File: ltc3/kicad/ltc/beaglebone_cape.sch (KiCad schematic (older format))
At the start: 13 parts, among them P301 BeagleBone_Black_Expansion_He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, P302 BeagleBone_Black_Expansion_He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, P303 JST PH header, P304 JST PH header, U301 CAT24C256

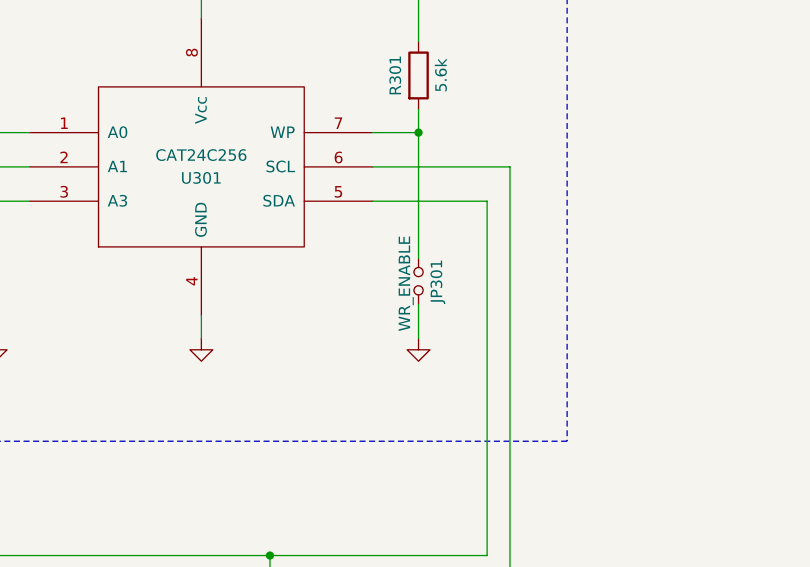
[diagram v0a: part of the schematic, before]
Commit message: LTC3: LTC schematic changes; LTC BOM work.
* Replaced LTC external power and trigger circuits' off-board manual
  override switches with board-mounted tactile momentary switches.
  Simplifies assembly, and should be more than adequate for debugging
  purposes.

* Changed cell protection diodes D1 and D6 from Rohm 1SS355 to ComChip
  CDSU4148.  CDSU4148 is already used on the LTC board, and is higher
  spec than the 1SS355.
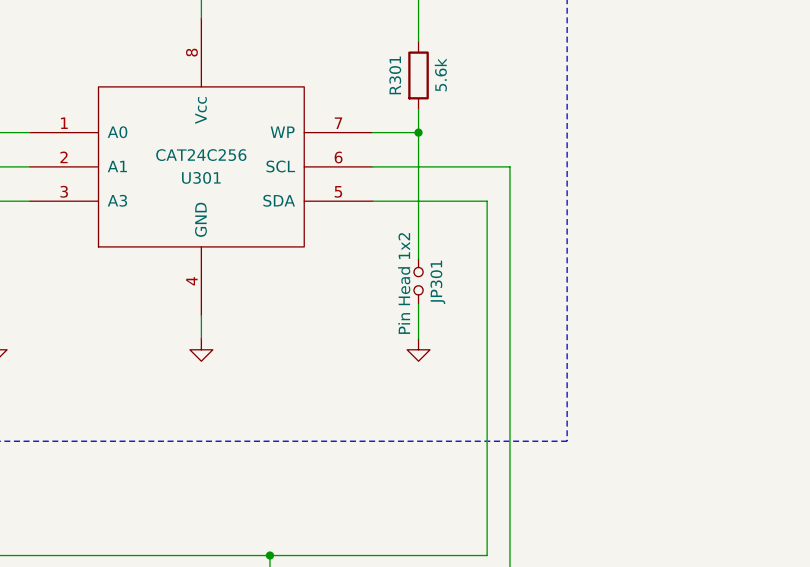
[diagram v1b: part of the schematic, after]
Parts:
- JP301: value WR_ENABLE -> Pin Head 1x2; Note Pin Header, 1x2 -> WR_ENABLE
- U301: Mfg_Name ON -> ON Semi

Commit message: LTC3: More work on LTC BOM.
Almost there!
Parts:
- P303: value JST PH header -> XH header; footprint Connectors_JST:JST_PH_B4B-PH-K_02x2.00mm_Straight -> Connectors_JST:JST_XH_B04B-XH-A_02x2.50mm_Straight; Mfg_Description - -> 4 pos vertical header; Mfg_PN B4B-PH-K-S -> B4B-XH-A(LF)(SN); Note To Charge Controller -> to charge controller
- P304: value JST PH header -> XH header; footprint Connectors_JST:JST_PH_B4B-PH-K_02x2.00mm_Straight -> Connectors_JST:JST_XH_B04B-XH-A_02x2.50mm_Straight; Mfg_Description - -> 4 pos vertical header; Mfg_PN B4B-PH-K-S -> B4B-XH-A(LF)(SN); Note To Cell Protection -> to cell protection
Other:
- note added: "TODO: add off-board JST XH connectors"
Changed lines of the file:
@@
 P 15800 6250
 F 0 "P303" H 15800 6500 50  0000 C CNN
-F 1 "JST PH header" V 15950 6250 50  0000 C CNN
-F 2 "Connectors_JST:JST_PH_B4B-PH-K_02x2.00mm_Straight" H 15800 6250 50  0001 C CNN
-F 3 "https://github.com/psas/launch-tower/blob/master/ltc3/doc/datasheets/connectors/JST-PH_connector.pdf" H 15800 6250 50  0001 C CNN
-F 4 "-" H 0   0   50  0001 C CNN "Mfg_Description"
+F 1 "XH header" V 15950 6250 50  0000 C CNN
+F 2 "Connectors_JST:JST_XH_B04B-XH-A_02x2.50mm_Straight" H 15800 6250 50  0001 C CNN
+F 3 "https://github.com/psas/launch-tower/blob/master/ltc3/doc/datasheets/connectors/JST-XH-2.5mm_pitch_Disconnectable_Crimp_style_connectors.pdf" H 15800 6250 50  0001 C CNN
+F 4 "4 pos vertical header" H 0   0   50  0001 C CNN "Mfg_Description"
 F 5 "JST" H 15800 6250 60  0001 C CNN "Mfg_Name"
-F 6 "B4B-PH-K-S" H 15800 6250 60  0001 C CNN "Mfg_PN"
-F 7 "To Charge Controller" V 16050 6250 50  0000 C CNN "Note"
+F 6 "B4B-XH-A(LF)(SN)" H 15800 6250 60  0001 C CNN "Mfg_PN"
+F 7 "to charge controller" V 16050 6250 50  0000 C CNN "Note"
 F 8 "-" H 15800 6250 60  0001 C CNN "Spec"
 	1    15800 6250
@@
 P 15800 7350
 F 0 "P304" H 15800 7600 50  0000 C CNN
-F 1 "JST PH header" V 15950 7350 50  0000 C CNN
-F 2 "Connectors_JST:JST_PH_B4B-PH-K_02x2.00mm_Straight" H 15800 7350 50  0001 C CNN
-F 3 "https://github.com/psas/launch-tower/blob/master/ltc3/doc/datasheets/connectors/JST-PH_connector.pdf" H 15800 7350 50  0001 C CNN
-F 4 "-" H 0   0   50  0001 C CNN "Mfg_Description"
+F 1 "XH header" V 15950 7350 50  0000 C CNN
+F 2 "Connectors_JST:JST_XH_B04B-XH-A_02x2.50mm_Straight" H 15800 7350 50  0001 C CNN
+F 3 "https://github.com/psas/launch-tower/blob/master/ltc3/doc/datasheets/connectors/JST-XH-2.5mm_pitch_Disconnectable_Crimp_style_connectors.pdf" H 15800 7350 50  0001 C CNN
+F 4 "4 pos vertical header" H 0   0   50  0001 C CNN "Mfg_Description"
 F 5 "JST" H 15800 7350 60  0001 C CNN "Mfg_Name"
-F 6 "B4B-PH-K-S" H 15800 7350 60  0001 C CNN "Mfg_PN"
-F 7 "To Cell Protection" V 16050 7350 50  0000 C CNN "Note"
+F 6 "B4B-XH-A(LF)(SN)" H 15800 7350 60  0001 C CNN "Mfg_PN"
+F 7 "to cell protection" V 16050 7350 50  0000 C CNN "Note"
 F 8 "-" H 15800 7350 60  0001 C CNN "Spec"
 	1    15800 7350
@@
 Text Label 8000 6300 2    60   ~ 0
 GPIO1_16
+Text Notes 12000 7650 0    100  Italic 20
+TODO: add off-board JST XH connectors
 Wire Notes Line
 	12550 4600 12550 2200
